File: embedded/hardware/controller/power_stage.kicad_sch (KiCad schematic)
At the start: 6 parts

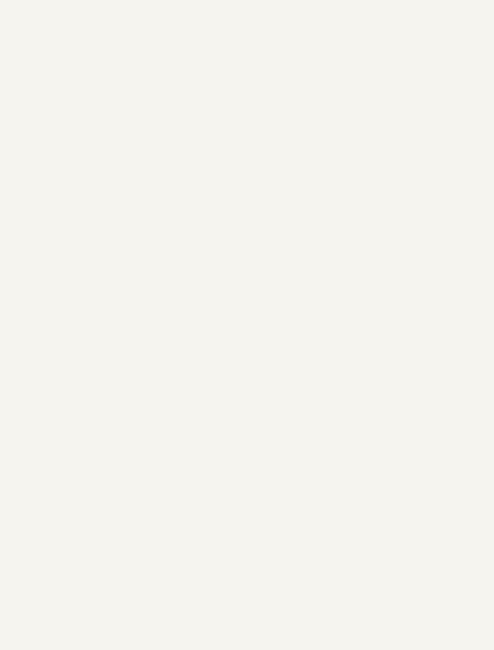
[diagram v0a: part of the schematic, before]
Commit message: Change for a bigger MCU, add place multiplexer for USART
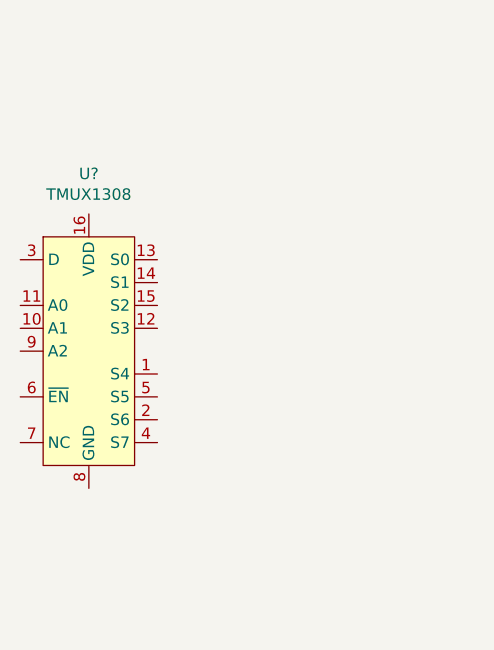
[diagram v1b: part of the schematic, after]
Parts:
- added U?: TMUX1308, Package_SO:TSSOP-16_4.4x5mm_P0.65mm, symbol User:TMUX1308
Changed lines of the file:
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@@
+    )
+  )
+  (symbol (lib_id "User:TMUX1308") (at 88.9 83.82 0) (unit 1)
+    (in_bom yes) (on_board yes)
+    (property "Reference" "U?" (id 0) (at 88.9 64.1158 0))
+    (property "Value" "TMUX1308" (id 1) (at 88.9 66.4145 0))
+    (property "Footprint" "Package_SO:TSSOP-16_4.4x5mm_P0.65mm" (id 2) (at 88.9 83.82 0)
+      (effects (font (size 1.27 1.27)) hide)
+    )
+    (property "Datasheet" "https://www.ti.com/lit/ds/symlink/tmux1308.pdf" (id 3) (at 88.9 83.82 0)
+      (effects (font (size 1.27 1.27)) hide)
     )
   )
